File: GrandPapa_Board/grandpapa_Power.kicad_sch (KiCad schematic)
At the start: 33 parts, among them U1 LT1576IS8-5#TRPBF, U2 TPS61023DRLT, U5 FPF2124, U6 INA180

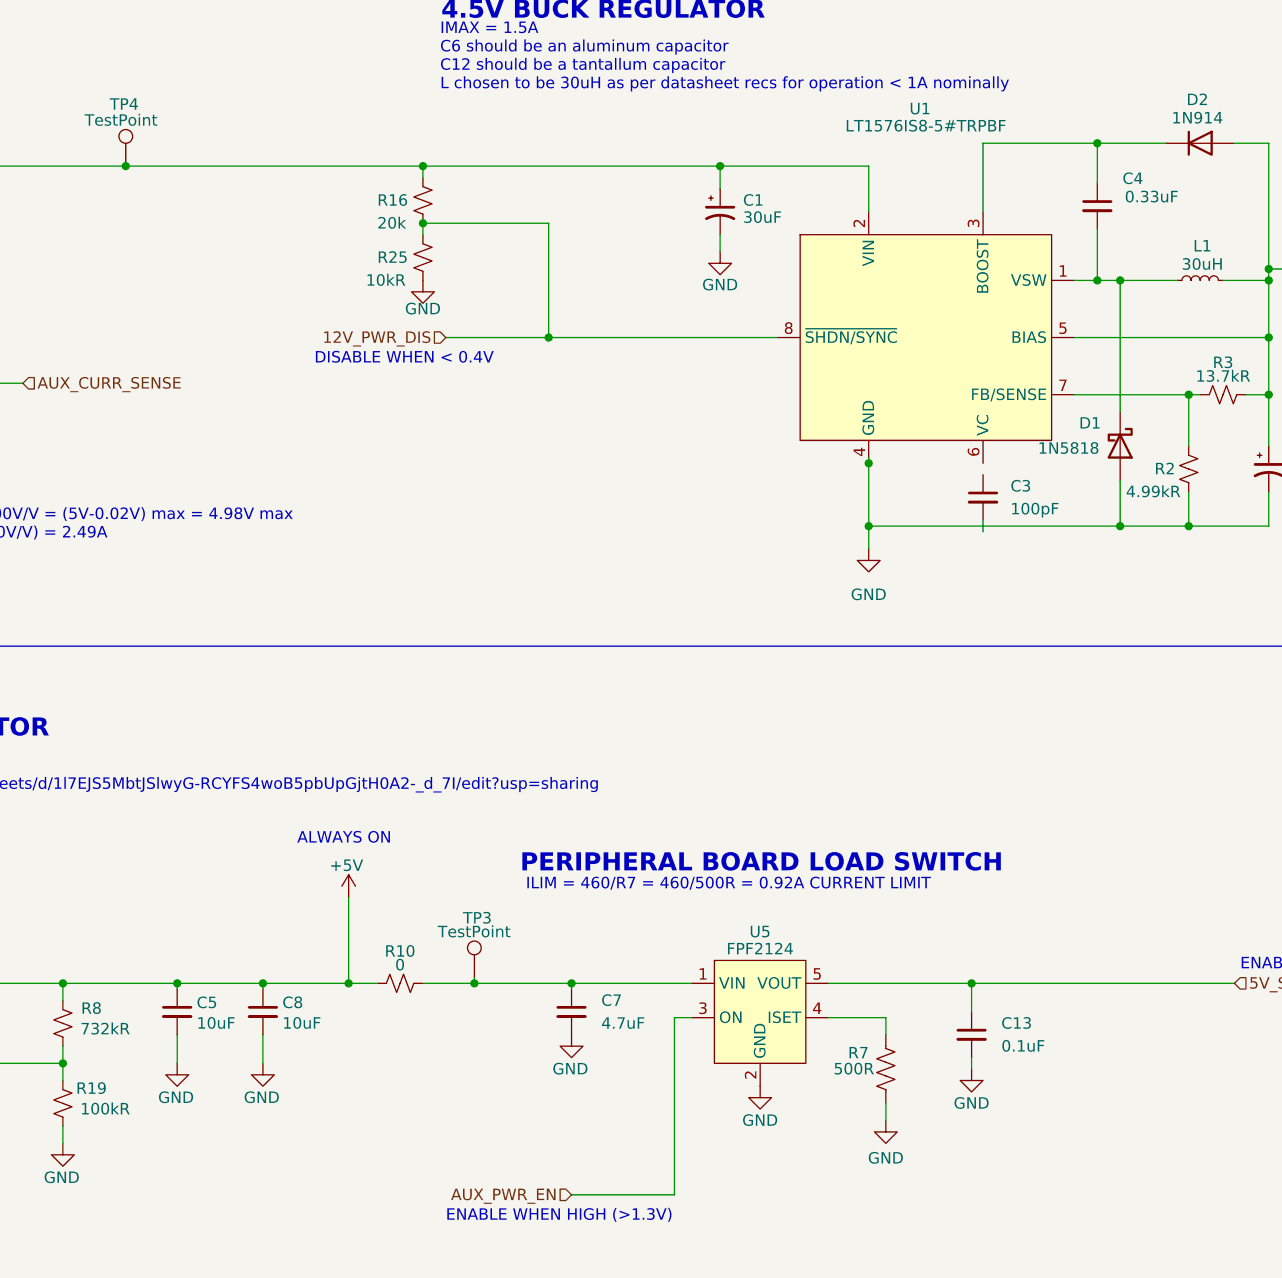
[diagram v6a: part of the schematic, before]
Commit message: fix disconnected pins, connect new hierarchical pins, misc layout changes
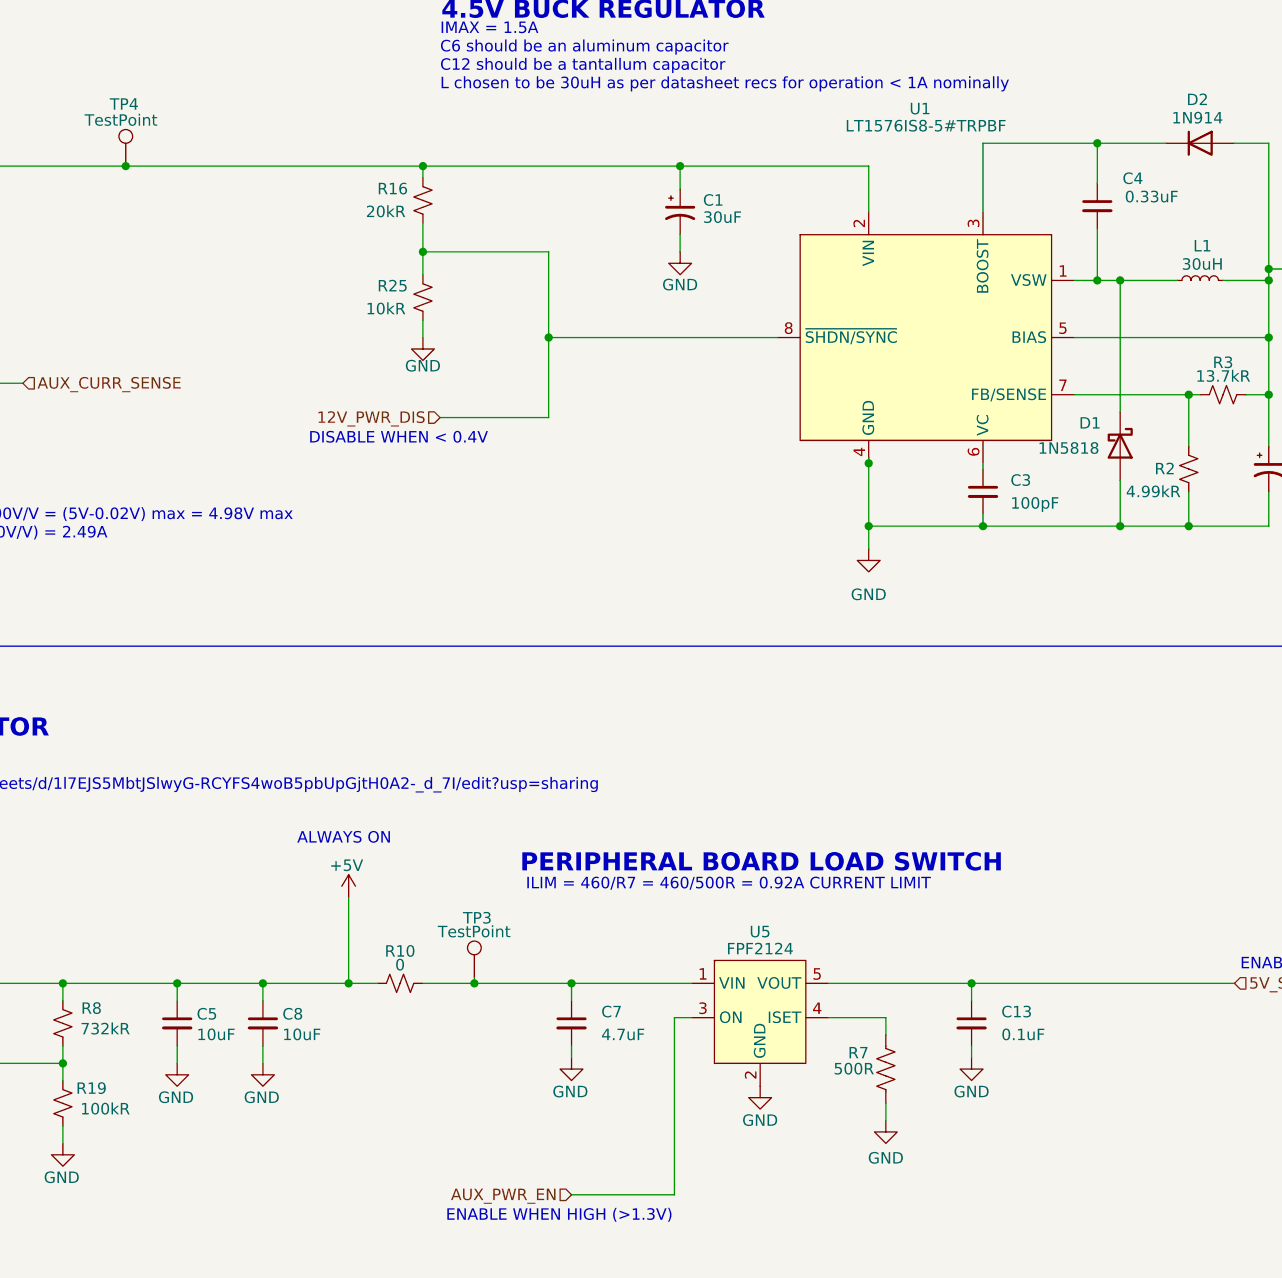
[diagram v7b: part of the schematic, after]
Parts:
- R16: value 20k -> 20kR
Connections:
- net GND: now also C3.2
- net at U1.6 (VC): now also C3.1
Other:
- moved on the sheet: C1, C13, C3, C5, C7, C8, R25
